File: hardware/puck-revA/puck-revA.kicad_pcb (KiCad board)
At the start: 2 copper layers, 50 x 50 mm, 39 parts, among them J1 USB-C 16P, J2 UART, J3 EXP (DNP on the product), SW1 BOOT, SW2 RESET, SW3 USER, U1 ESP32-S3-WROOM-1U-N16, U2 AP2112K-3.3, U3 74AHCT1G125, U4 USBLC6-2SC6, U5 ambient light, DNP

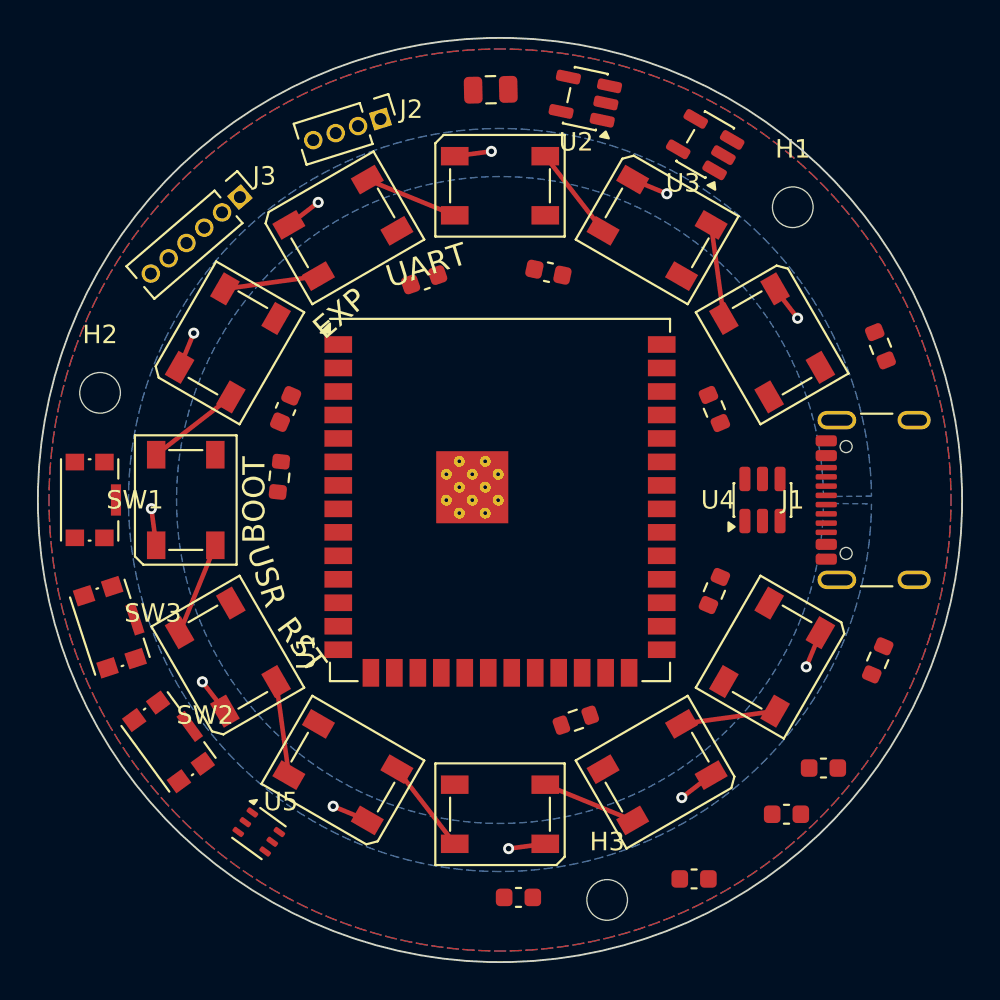
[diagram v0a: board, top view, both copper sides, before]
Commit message: Update design rules for clearance and hole dimensions in puck-revA
- Adjusted minimum clearance from 0.15 to 0.127
- Updated minimum hole clearance from 0.25 to 0.127
- Changed minimum through hole diameter from 0.3 to 0.15
- Modified minimum track width from 0.15 to 0.127
- Reduced minimum via annular width from 0.1 to 0.05
- Decreased minimum via diameter from 0.45 to 0.25
- Updated net settings clearance to match new design rules
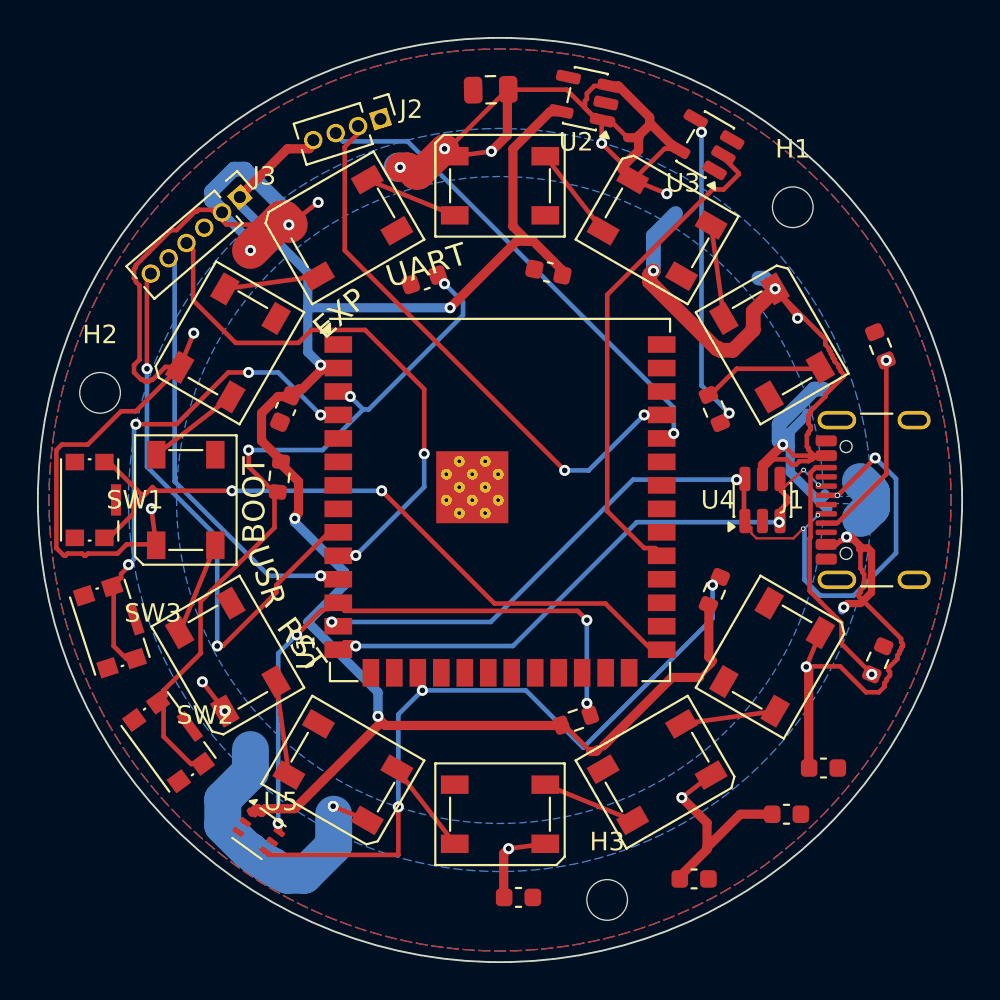
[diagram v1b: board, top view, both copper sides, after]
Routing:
- net VBUS: track 22.0 -> 221.3 mm, vias 11 -> 22
- net +3V3: track 0.00 -> 100.5 mm, vias 0 -> 4
- net USB_DM: track 0.00 -> 51.4 mm, vias 0 -> 6
- net EN: track 0.00 -> 40.7 mm, vias 0 -> 3
- net SCL: track 0.00 -> 40.0 mm, vias 0 -> 3
- net IO0: track 0.00 -> 38.3 mm, vias 0 -> 2
- net SDA: track 0.00 -> 33.3 mm, vias 0 -> 4
- net USB_DP: track 0.00 -> 33.1 mm, vias 0 -> 4
- net EXP_C: track 0.00 -> 31.0 mm, vias 0 -> 2
- net UART0_TX: track 0.00 -> 30.4 mm, vias 0 -> 2
- net EXP_A: track 0.00 -> 29.9 mm, vias 0 -> 2
- net LED_DATA_3V3: track 0.00 -> 27.0 mm
- net USER_BTN: track 0.00 -> 26.9 mm, vias 0 -> 4
- net UART0_RX: track 0.00 -> 26.6 mm, vias 0 -> 1
- net EXP_B: track 0.00 -> 23.3 mm, vias 0 -> 1
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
